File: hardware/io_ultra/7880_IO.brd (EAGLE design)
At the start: 167.9 x 122.5 mm, 64 parts, among them IC11 74HCT245DW, IC4 74HCT139N, IC5 74AC06N, IC7 MAX232, J1 DIN5, X2 CRYSTALS-NOGND-CFPX-217, X3 22-23-2021, X4 CRYSTALS-NOGND-CFPX-217

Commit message: I/O ultra board updated
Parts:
- removed X1: (no value), con-subd:M09HP
- added C11, C28, C29, C30: (no value), rcl:C0603
- added IC6: MAX232, maxim:DIL16
- added SV1, SV3: (no value), con-ml:ML10
- C2: device rcl:C1206 -> rcl:C0603
- moved C3 125.4 mm to (32.1, 104.8)
- moved C2 91.3 mm to (21.0, 69.0)
- moved C6 9.42 mm to (14.0, 101.6), turned to 180 degrees
- moved C17 4.13 mm to (83.1, 61.6), turned to 180 degrees
- moved C10 3.93 mm to (21.0, 101.6), turned to 180 degrees
- moved C25 2.01 mm to (6.99, 88.9)
- moved X3 2.01 mm to (14.0, 112.4)
- moved C5 2.01 mm to (7.37, 93.1)
- moved IC7 2.01 mm to (14.0, 92.7)
- moved C4 0.67 mm to (7.37, 99.1)
- moved BATTERY_1 0.64 mm to (13.3, 34.9)
- moved QG1 0.64 mm to (28.3, 99.7)
- moved R11 0.64 mm to (28.3, 107.3)
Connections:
- removed net CTS1: IC7.9
- removed net N$7: IC7.7, X1.7
- removed net RTS1: IC7.10
- new net CTS1_TTL: IC2.7, IC7.9
- new net CTS2_TTL: IC2.4, IC6.9
- new net N$15: IC6.7, SV3.4
- new net N$16: C11.2, IC6.1
- new net N$26: C28.2, IC6.4
- new net N$27: C28.1, IC6.5
- new net N$30: C11.1, IC6.3
- new net N$31: C29.1, IC6.2
- new net N$36: IC6.13, SV3.3
- new net N$38: IC6.14, SV3.5
- new net N$39: IC6.8, SV3.2
- new net N$40: C30.1, IC6.6
- new net N$41: IC7.7, SV1.4
- new net RTS1_TTL: IC2.29, IC7.10
- new net RTS2_TTL: IC2.12, IC6.10
- new net RXD2_TTL: IC2.10, IC6.12
- new net TXD2_TTL: IC2.11, IC6.11
- net GND: now also C30.2, IC6.15, SV1.9, SV3.9; no longer X1.5
- net N$18: now also SV1.5; no longer X1.3
- net N$28: now also SV1.2; no longer X1.8
- net N$8: now also SV1.3; no longer X1.2
- net VCC: now also C29.2, IC6.16
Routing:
- net CTS2_TTL: track 0.00 -> 72.1 mm, vias 0 -> 2
- net VCC: track 642.5 -> 712.1 mm, vias 22 -> 24
- net RXD2_TTL: track 0.00 -> 44.7 mm, vias 0 -> 2
- net TXD2_TTL: track 0.00 -> 43.9 mm, vias 0 -> 2
- net RTS2_TTL: track 0.00 -> 43.4 mm, vias 0 -> 2
- net CTS1_TTL: track 0.00 -> 41.0 mm, vias 0 -> 2
- net RTS1_TTL: track 0.00 -> 35.8 mm
- net N$18: track 0.00 -> 27.9 mm
- net N$38: track 0.00 -> 27.9 mm
- net N$8: track 0.00 -> 21.4 mm
- net N$36: track 0.00 -> 21.0 mm
- net TXD1_TTL: track 18.0 -> 35.8 mm
- net RXD1_TTL: track 18.0 -> 35.8 mm
- net UART_RX_IRQ: track 79.8 -> 64.7 mm, vias 4 -> 2
- net N$41: track 0.00 -> 9.04 mm
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
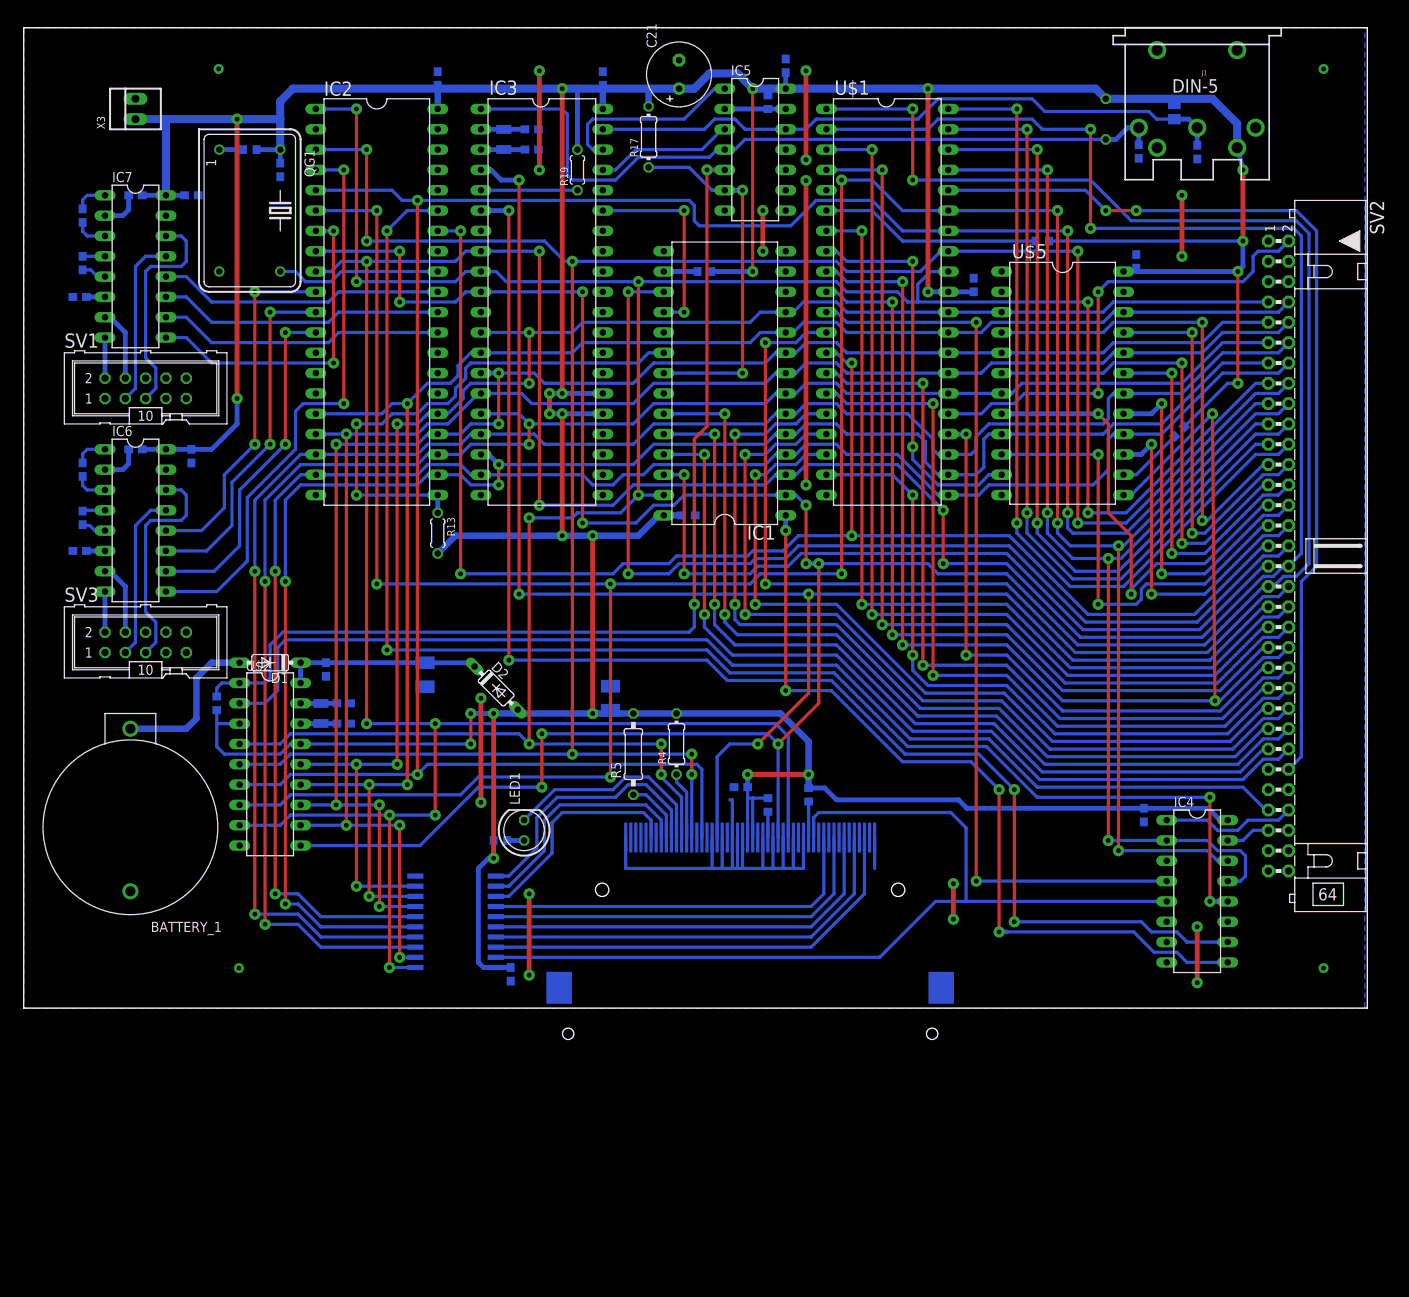
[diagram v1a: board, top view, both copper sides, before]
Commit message: I/O board (Ultra version) bug fixes
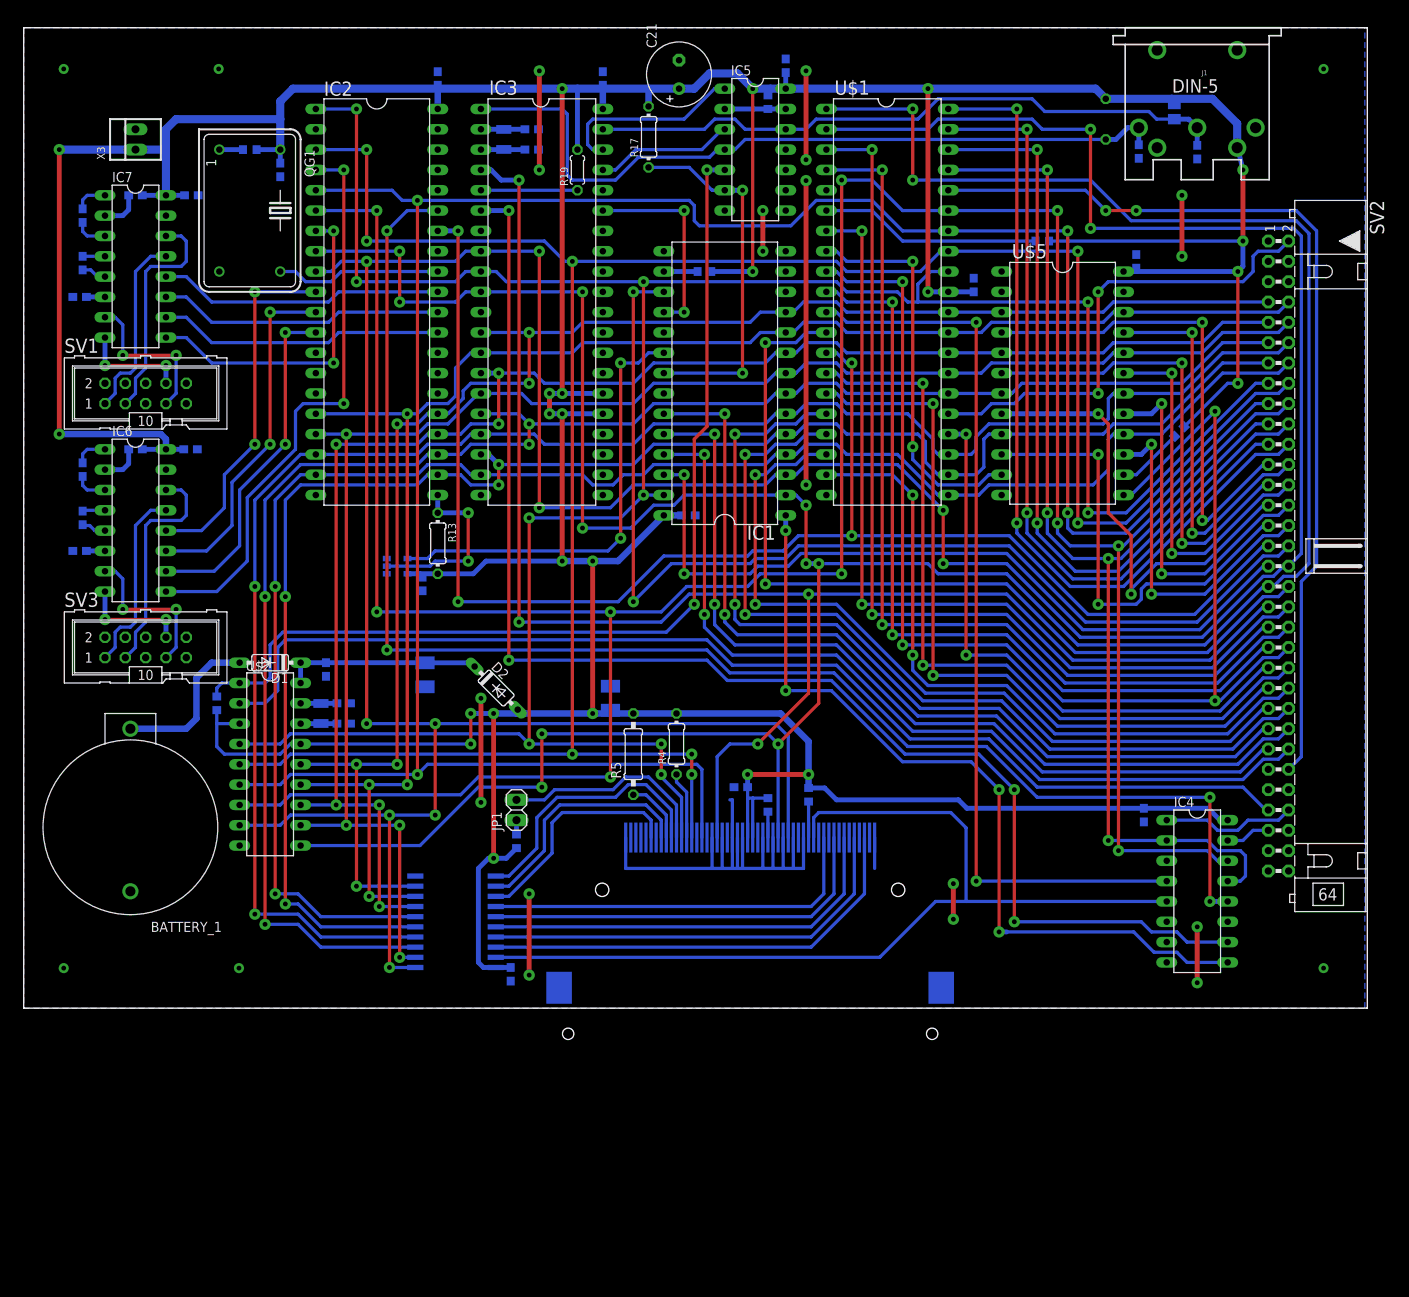
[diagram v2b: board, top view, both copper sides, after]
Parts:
- removed LED1: (no value), led:LED5MM
- added C31: 100N, rcl:C0603
- added IC8: 74LVC1G04DBV, 74xx-little-us:SOT23-5
- added JP1: (no value), pinhead:1X02
- R13: device rcl:0204/5 -> rcl:0204/7
- moved X3 3.81 mm to (14.0, 108.6)
- moved R16 2.01 mm to (61.6, 20.9), turned to 270 degrees
- moved R13 1.27 mm to (51.8, 58.1)
- moved C2 0.86 mm to (20.9, 69.8), turned to 180 degrees
- moved SV1 0.64 mm to (15.2, 76.8)
- moved SV3 0.63 mm to (15.2, 45.1)
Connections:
- removed net N$28: IC7.8, SV1.2
- removed net N$41: IC7.7, SV1.4
- new net COM1_CTS: IC7.8, SV1.8
- new net COM1_RXD: IC7.13, SV1.1
- new net COM1_TXD: IC7.14, SV1.3
- net GND: now also C31.2, IC8.3, SV1.5, SV3.5; no longer SV1.9, SV3.9
- net N$15: now also SV3.7; no longer SV3.4
- net N$18: now also IC7.7, SV1.7; no longer IC7.14, SV1.5
- net N$33: now also JP1.2; no longer LED1.K
- net N$34: now also JP1.1; no longer LED1.A
- net N$36: now also SV3.1; no longer SV3.3
- net N$38: now also SV3.3; no longer SV3.5
- net N$39: now also SV3.8; no longer SV3.2
- net N$8: now also IC2.21, IC8.2, R13.1; no longer IC7.13, SV1.3
- net UART_RX_IRQ: now also IC8.4; no longer IC2.21, R13.1
- net VCC: now also C31.1, IC8.5
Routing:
- net COM1_TXD: track 0.00 -> 28.5 mm
- net COM1_RXD: track 0.00 -> 23.4 mm
- net VCC: track 712.1 -> 731.7 mm
- net COM1_CTS: track 0.00 -> 13.3 mm, vias 0 -> 2
- net N$15: track 9.04 -> 19.7 mm, vias 0 -> 2
- net UART_RX_IRQ: track 64.7 -> 55.5 mm
- net N$41: track 9.04 -> 0.00 mm
- net N$39: track 5.08 -> 13.3 mm, vias 0 -> 2
- net N$18: track 27.9 -> 19.7 mm, vias 0 -> 2
- net N$28: track 5.08 -> 0.00 mm
- net RESET: track 181.6 -> 186.5 mm
- net !RESET: track 194.1 -> 199.0 mm
- net INT: track 131.6 -> 135.2 mm
- net N$36: track 21.0 -> 23.4 mm
- net RTC_IRQ: track 126.3 -> 124.7 mm
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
